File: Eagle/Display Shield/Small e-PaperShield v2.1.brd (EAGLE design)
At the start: 172.6 x 54.6 mm, 141 parts, among them J2 3300060P1-ST-TF-003A, J3 2.54-8p-male-SMD, J4 2.54-8p-male-SMD, J5 2.54-6p-male-SMD, J6 2.54-6p-male-SMD, J7 2.54-2x3p-female-SMD, Q10 MOSFET-P-044021001, Q11 2N7002, Q2 2N7002, Q3 MOSFET-P-044021001, Q5 MOSFET-P-044021001, Q7 MOSFET-P-044021001, Q8 2N7002, Q9 2N7002, SW1 BUTTON-4P-REINFORCE'TS-1188E', U2 XC6206-3.3-1300260P1, U3 74VHC125PW, U4 74VHC125PW, U5 GT20L16P1Y, U6 DNP, U7 EPD 1.44/2.0/2.7 inch, U8 DNP, U9 S-8120CNB-DRB-TF-G//200021001

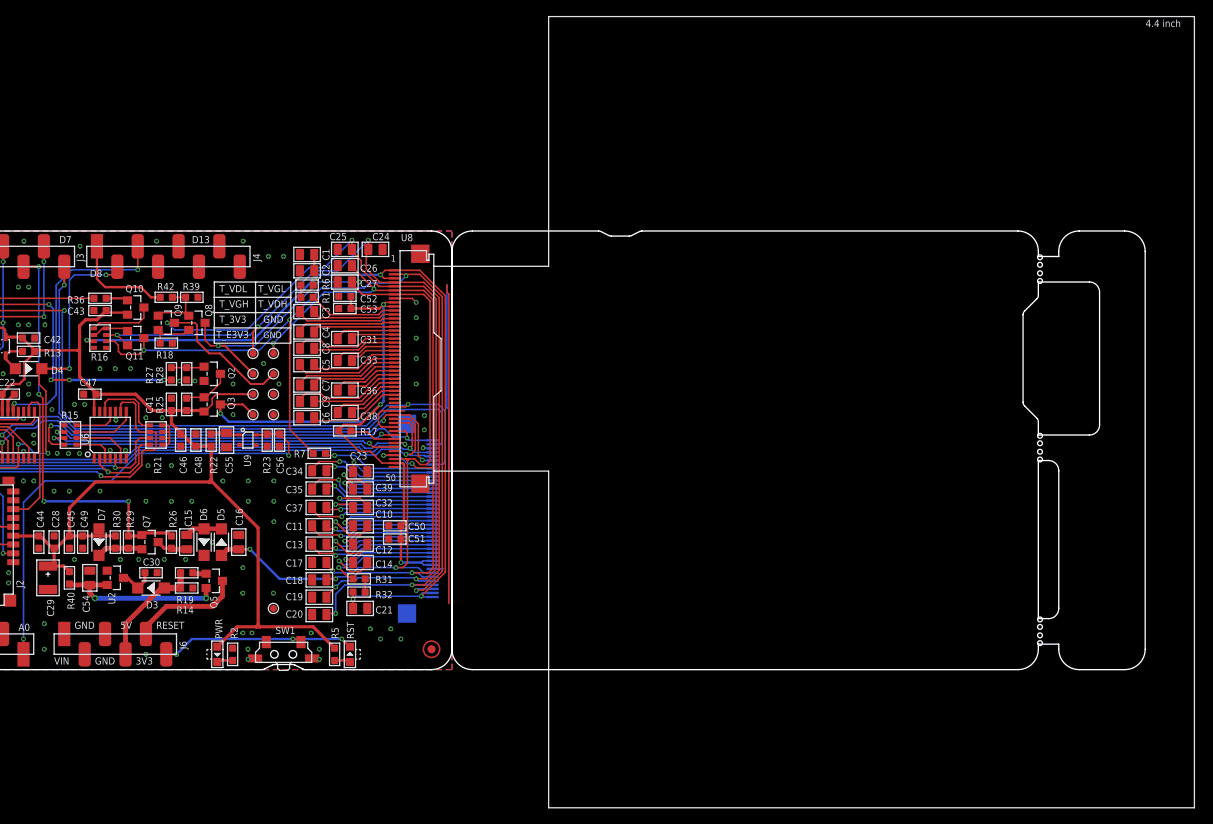
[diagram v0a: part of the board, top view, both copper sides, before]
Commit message: removed all unnecessary components of display shield
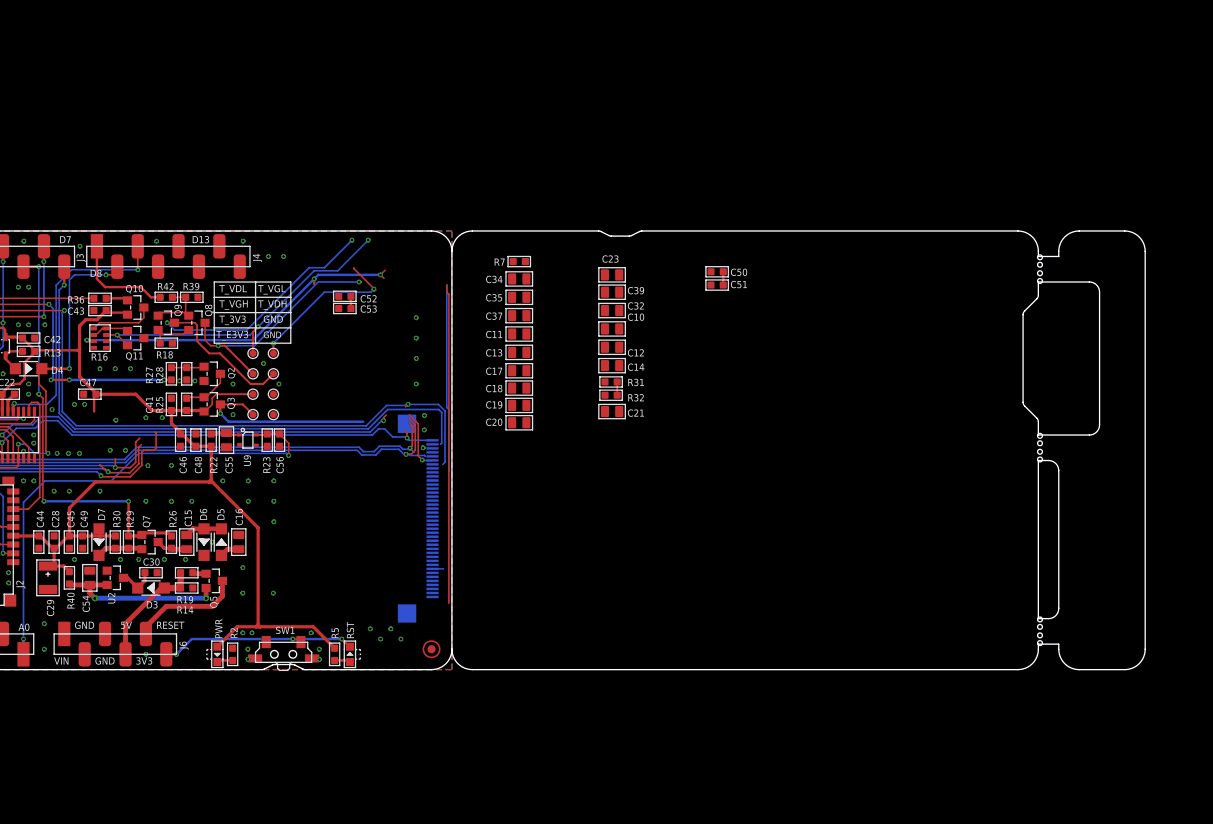
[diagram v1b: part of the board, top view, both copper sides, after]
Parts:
- removed C1, C2, C24, C25, C26, C27, C3, C31, C33, C36, C38, C4, C5, C6, C7, C8, C9: DNP, Discrete:C0805
- removed R1, R17, R6: DNP, Discrete:R0603
- removed R15, R21: DNP, Discrete:1206-8-3.3X2.4
- removed TP8: (no value), Discrete:TP_3535
- removed U6: DNP, IC:TSSOP14
- removed U8: DNP, template:50P-0.5
- moved C50 51.1 mm to (57.8, 22.2)
- moved C51 51.1 mm to (57.8, 20.6)
- moved C10 39.8 mm to (44.7, 15.1)
- moved C12 39.8 mm to (44.7, 12.8)
- moved C14 39.8 mm to (44.7, 10.5)
- moved C21 39.8 mm to (44.7, 4.83)
- moved C23 39.8 mm to (44.7, 21.8)
- moved C32 39.8 mm to (44.7, 17.4)
- moved C39 39.8 mm to (44.7, 19.7)
- moved R31 39.8 mm to (44.6, 8.51)
- moved R32 39.8 mm to (44.6, 6.86)
- moved C17 34.5 mm to (33.1, 9.91)
- moved C18 34.5 mm to (33.1, 7.75)
- moved C19 34.5 mm to (33.1, 5.59)
- moved C35 34.5 mm to (33.1, 19.1)
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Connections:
- removed net EPD_CKV: R15.7, U8.44
- removed net EPD_OE123: R15.8, U8.42
- removed net EPD_STV_IN: R15.6, U8.45
- removed net N$15: C4.1, U8.14
- removed net N$19: R21.5, U6.12
- removed net N$23: R15.1, U6.3
- removed net N$24: R15.3, U6.8
- removed net N$25: R15.4, U6.11
- removed net N$26: R15.2, U6.6
- removed net N$30: R1.2, R6.1
- removed net N$33: R15.5
- removed net N$39: C4.2, U8.15
- removed net N$40: C3.1, U8.12
- removed net N$41: C31.2, U8.17
- removed net N$42: C31.1, U8.16
- removed net N$43: C8.1, U8.18
- removed net N$44: C8.2, U8.19
- removed net N$45: C33.2, U8.21
- removed net N$46: C33.1, U8.20
- removed net N$47: C5.1, U8.22
- removed net N$48: C5.2, U8.23
- removed net N$49: C7.1, U8.24
- removed net N$50: C7.2, U8.25
- removed net N$51: C36.1, U8.26
- removed net N$52: C36.2, U8.27
- removed net N$53: C9.1, U8.28
- removed net N$54: C9.2, U8.29
- removed net N$55: C38.1, U8.30
- removed net N$56: C38.2, U8.31
- removed net N$57: C6.1, U8.32
- removed net N$58: R1.1, U8.11
- removed net N$67: R17.1, U8.43
- removed net N$82: C3.2, U8.13
- net /EPD_CS: no longer U8.41
- net EPD_/RESET: no longer U8.35
- net EPD_BORDER: no longer U8.2
- net EPD_SO: no longer U8.37
- net EPD_VCOM_PANEL: no longer C1.1, C2.1, R6.2, U8.1, U8.3
- net EPD_VDH: no longer C25.1, U8.5
- net EPD_VDL: no longer C24.1, U8.4
- net EPD_VGH: no longer C27.1, U8.48, U8.7
- net EPD_VGL: no longer C26.1, U8.47, U8.6
- net GND: no longer C1.2, C2.2, C24.2, C25.2, C26.2, C27.2, C6.2, R21.1, R21.2, R21.3, R21.4, TP8.T, U6.1, U6.10, U6.13, U6.4, U6.7, U8.36, U8.40, U8.50, U8.8, U8.P1, U8.P2
- net M_CKV: no longer R21.7, U6.5
- net M_OE123: no longer R21.8, U6.2
- net M_STV_IN: no longer R21.6, U6.9
- net S_MOSI: no longer U8.38
- net S_SCK: no longer U8.39
- net VCC_3V3: no longer U6.14
- net VCC_3V3_EPD: no longer R17.2, U8.10, U8.49, U8.9
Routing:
- net EPD_BORDER: track 109.7 -> 0.00 mm, vias 4 -> 0
- net EPD_VGL: track 103.0 -> 23.0 mm, vias 7 -> 2
- net EPD_VDL: track 111.9 -> 43.3 mm, vias 5 -> 3
- net EPD_VGH: track 96.8 -> 30.7 mm, vias 4 -> 2
- net EPD_VDH: track 112.1 -> 46.1 mm, vias 4 -> 2
- net EPD_VCOM_PANEL: track 108.8 -> 42.9 mm, vias 5 -> 3
- net VCC_3V3_EPD: track 82.8 -> 27.1 mm, vias 4 -> 1
- net EPD_OE123: track 47.8 -> 0.00 mm, vias 2 -> 0
- net EPD_CKV: track 47.1 -> 0.00 mm, vias 2 -> 0
- net EPD_STV_IN: track 43.9 -> 0.00 mm, vias 2 -> 0
- net N$97: track 18.0 -> 0.00 mm, vias 1 -> 0
- net N$93: track 18.0 -> 0.00 mm, vias 1 -> 0
- net N$101: track 17.1 -> 0.00 mm, vias 1 -> 0
- net N$81: track 16.6 -> 0.00 mm, vias 1 -> 0
- net GND: track 85.3 -> 68.7 mm, vias 113 -> 112
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
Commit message: re-placed components to board area, added 40pin connector. ready to go
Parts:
- added X1: FH12-40S-0.5SH, con-hirose:FH12-40S-0.5SH
- moved S5 203.7 mm to (84.5, 12.4)
- moved S6 203.7 mm to (74.7, 12.4)
- moved S7 203.7 mm to (64.9, 12.4)
- moved S8 203.7 mm to (55.1, 12.4)
- moved C11 76.2 mm to (85.5, 69.8)
- moved C13 76.2 mm to (85.5, 67.5)
- moved C17 76.2 mm to (85.5, 65.2)
- moved C18 76.2 mm to (85.5, 63.0)
- moved C19 76.2 mm to (85.5, 60.9)
- moved C20 76.2 mm to (85.5, 58.7)
- moved C34 76.2 mm to (85.5, 76.6)
- moved C35 76.2 mm to (85.5, 74.3)
- moved C37 76.2 mm to (85.5, 72.1)
- moved C15 75.1 mm to (47.6, 38.8)
- moved C16 75.1 mm to (54.1, 38.8)
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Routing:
- net /EPD_CS: track 67.1 -> 64.2 mm
- net GND: track 68.7 -> 67.3 mm
- net EPD_SO: track 61.5 -> 60.3 mm
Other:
- board size 172.6 x 54.6 mm -> 86.3 x 54.6 mm

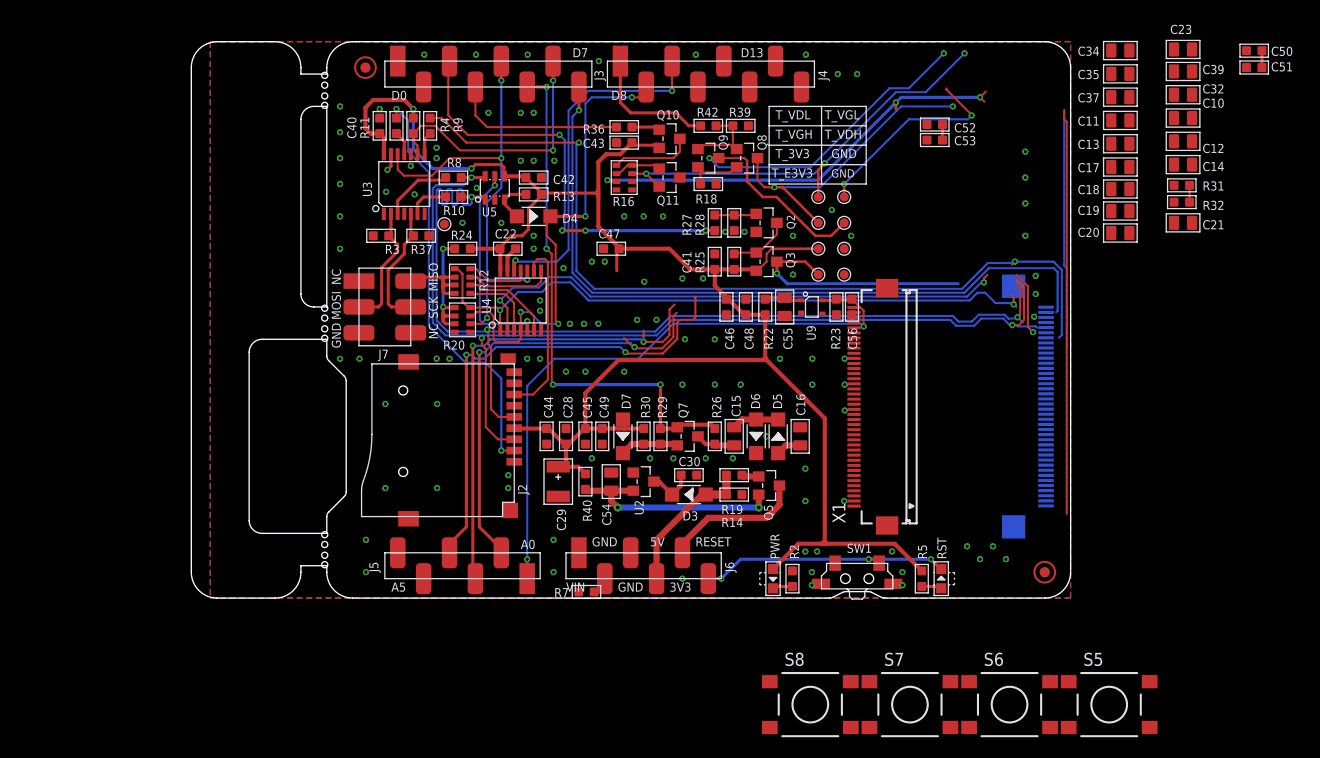
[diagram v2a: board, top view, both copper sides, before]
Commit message: reshaped board, snapped components to grid.
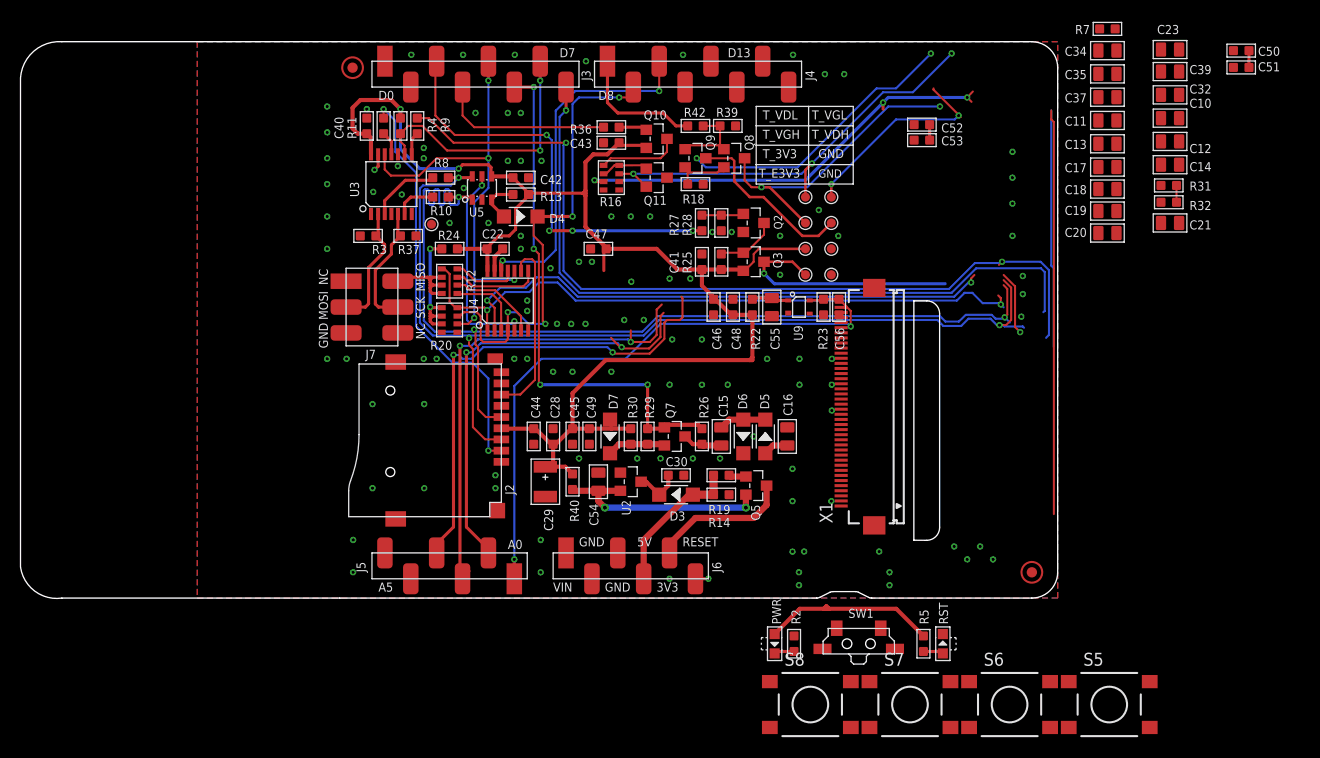
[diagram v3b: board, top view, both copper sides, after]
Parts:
- removed U7: EPD 1.44/2.0/2.7 inch, moudle:40P-0.5
- moved R7 75.3 mm to (84.3, 78.8)
- moved PWR 6.39 mm to (51.6, 18.4)
- moved R2 6.39 mm to (53.5, 18.4)
- moved R5 6.39 mm to (66.2, 18.4)
- moved RST 6.39 mm to (68.1, 18.4)
- moved SW1 6.39 mm to (59.9, 18.4)
- moved R31 1.28 mm to (90.3, 63.4)
- moved R32 1.28 mm to (90.3, 61.7)
- moved C10 1.28 mm to (90.4, 70.0)
- moved C12 1.28 mm to (90.4, 67.7)
- moved C14 1.28 mm to (90.4, 65.4)
- moved C21 1.28 mm to (90.4, 59.7)
- moved C23 1.28 mm to (90.4, 76.7)
- moved C32 1.28 mm to (90.4, 72.3)
- moved C39 1.28 mm to (90.4, 74.6)
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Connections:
- net /EPD_CS: now also X1.40; no longer U7.1
- net ADC_IN: now also X1.33; no longer U7.8
- net EPD_/RESET: now also X1.34; no longer U7.7
- net EPD_BORDER: now also X1.3; no longer U7.38
- net EPD_SO: now also X1.35; no longer U7.6
- net EPD_VCL: now also X1.32; no longer U7.9
- net EPD_VCOM_PANEL: now also X1.1, X1.2; no longer U7.39, U7.40
- net EPD_VDH: now also X1.5; no longer U7.36
- net EPD_VDL: now also X1.4; no longer U7.37
- net EPD_VGH: now also X1.7; no longer U7.34
- net EPD_VGL: now also X1.6; no longer U7.35
- net GND: now also X1.38, X1.8; no longer U7.3, U7.33, U7.P1, U7.P2
- net M_EPD_BUSY: now also X1.39; no longer U7.2
- net N$100: now also X1.13; no longer U7.28
- net N$101: now also X1.12; no longer U7.29
- net N$34: now also X1.31; no longer U7.10
- net N$35: now also X1.30; no longer U7.11
- net N$36: now also X1.29; no longer U7.12
- net N$37: now also X1.28; no longer U7.13
- net N$81: now also X1.27; no longer U7.14
- net N$85: now also X1.26; no longer U7.15
- net N$88: now also X1.25; no longer U7.16
- net N$89: now also X1.24; no longer U7.17
- net N$90: now also X1.23; no longer U7.18
- net N$91: now also X1.22; no longer U7.19
- net N$92: now also X1.21; no longer U7.20
- net N$93: now also X1.20; no longer U7.21
- net N$94: now also X1.19; no longer U7.22
- net N$95: now also X1.18; no longer U7.23
- net N$96: now also X1.17; no longer U7.24
- net N$97: now also X1.16; no longer U7.25
- net N$98: now also X1.15; no longer U7.26
- net N$99: now also X1.14; no longer U7.27
- net S_MOSI: now also X1.36; no longer U7.5
- net S_SCK: now also X1.37; no longer U7.4
- net VCC_3V3_EPD: now also X1.10, X1.9; no longer U7.31, U7.32
- net VCOM_DRIVER: now also X1.11; no longer U7.30
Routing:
- net M_RESET: track 25.4 -> 1.27 mm, vias 3 -> 1
- net VCC_3V3: track 184.9 -> 164.4 mm
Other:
- board size 86.3 x 54.6 mm -> 101.8 x 54.6 mm

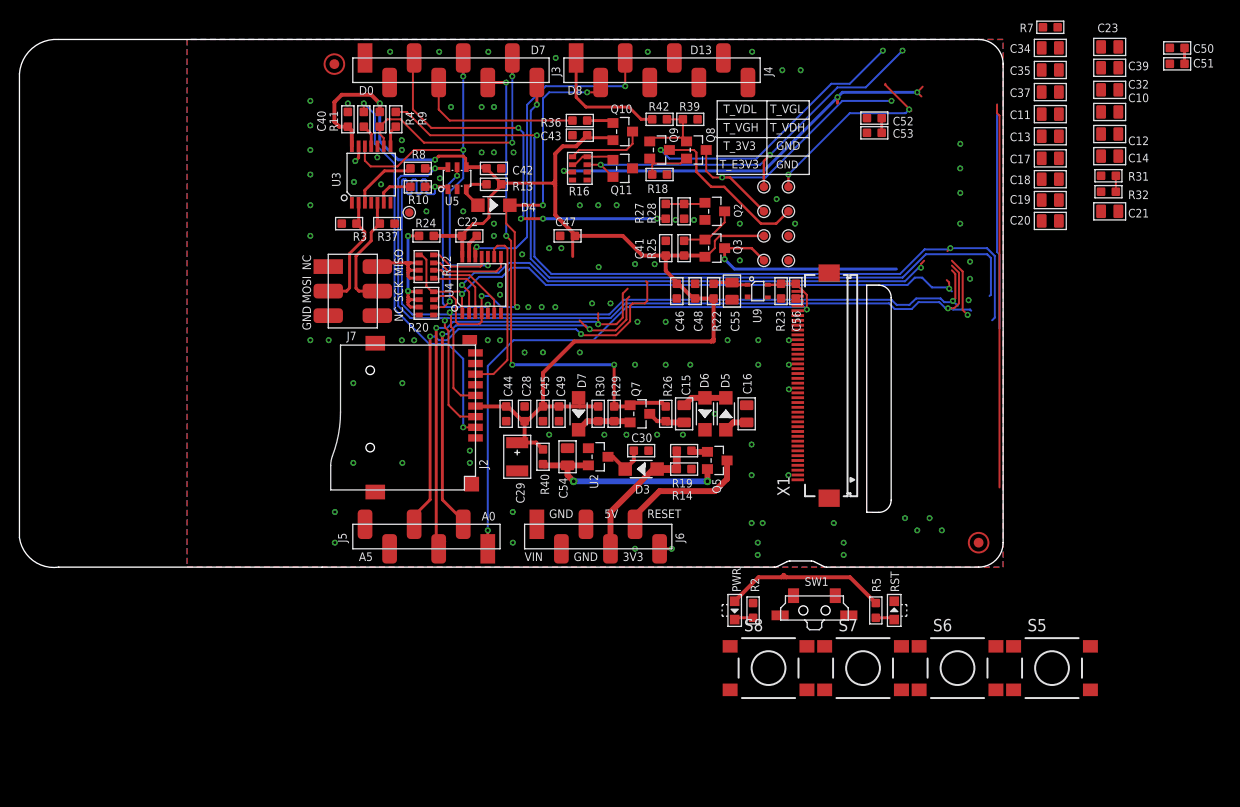
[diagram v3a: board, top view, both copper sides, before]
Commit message: re-routed most of the traces
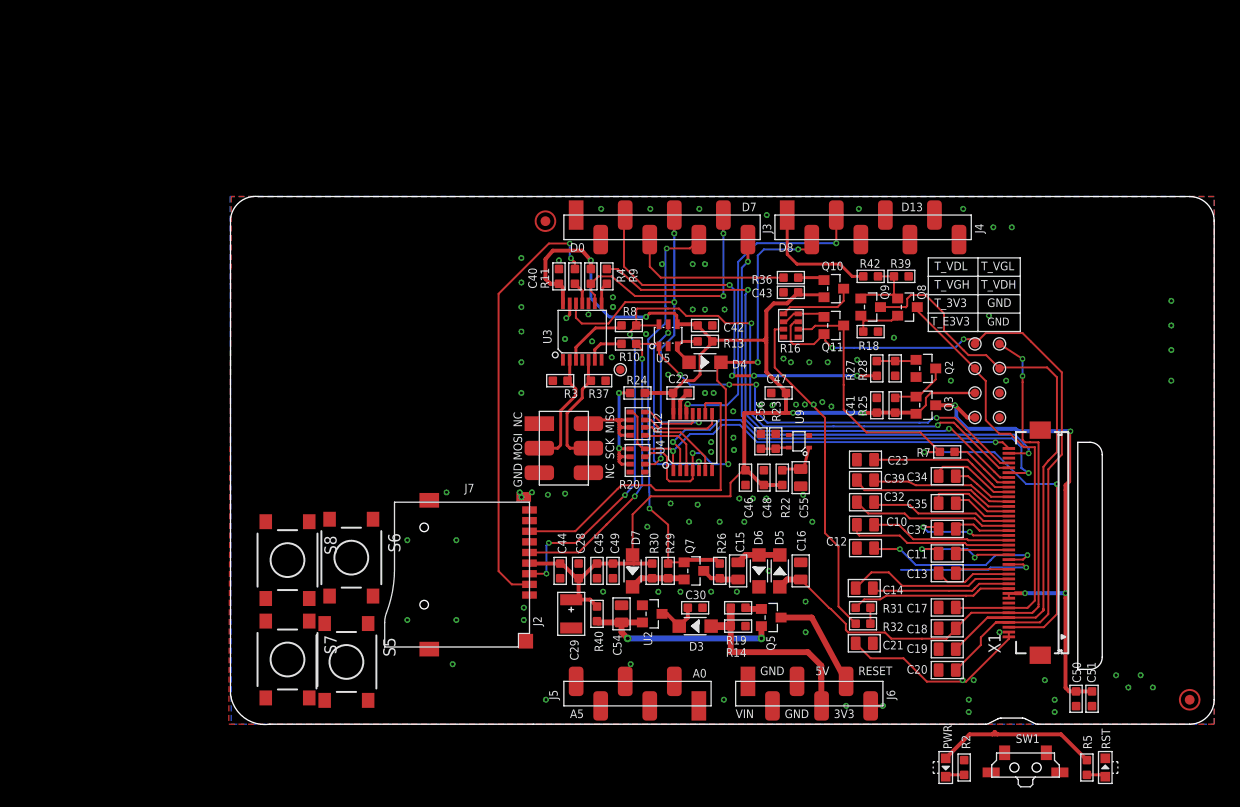
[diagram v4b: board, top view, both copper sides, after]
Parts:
- removed C52, C53: 100nF, Discrete:C0603
- moved S5 73.0 mm to (11.4, 13.1), turned to 270 degrees
- moved C50 68.2 mm to (86.9, 9.27), turned to 90 degrees
- moved C51 66.3 mm to (88.6, 9.27), turned to 90 degrees
- moved S6 63.8 mm to (11.9, 23.9), turned to 270 degrees
- moved S7 59.6 mm to (5.33, 13.3), turned to 270 degrees
- moved C14 51.4 mm to (65.0, 20.7)
- moved C21 51.4 mm to (65.0, 15.0)
- moved R31 51.4 mm to (64.9, 18.7)
- moved R32 51.4 mm to (64.9, 17.0)
- moved S8 51.0 mm to (5.33, 23.6), turned to 270 degrees
- moved C12 49.7 mm to (65.2, 24.9), turned to 180 degrees
- moved C23 49.6 mm to (65.2, 34.0), turned to 0 degrees
- moved C10 49.6 mm to (65.2, 27.3), turned to 180 degrees
- moved C32 49.6 mm to (65.2, 29.6)
- moved C39 49.6 mm to (65.2, 31.9)
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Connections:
- net GND: no longer C52.1, C53.1
- net VCC_3V3_EPD: no longer C52.2, C53.2
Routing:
- net GND: track 67.3 -> 4.16 mm, vias 112 -> 105
- net EPD_BORDER: track 0.00 -> 61.0 mm, vias 0 -> 2
- net M_TEMP_SEN: track 60.6 -> 2.92 mm, vias 2 -> 0
- net M_CKV: track 48.7 -> 0.00 mm, vias 2 -> 0
- net M_STV_IN: track 48.1 -> 0.00 mm, vias 2 -> 0
- net M_OE123: track 45.5 -> 0.00 mm, vias 2 -> 0
- net EPD_VGL: track 23.0 -> 61.4 mm
- net EPD_VDL: track 43.3 -> 74.6 mm, vias 3 -> 2
- net VCC_3V3_EPD: track 27.1 -> 56.0 mm, vias 1 -> 4
- net EPD_/RESET: track 85.3 -> 58.5 mm
- net S_SCK: track 100.5 -> 75.8 mm, vias 3 -> 6
- net M_EPD_BUSY: track 72.1 -> 52.2 mm, vias 1 -> 2
- net N$96: track 0.00 -> 19.1 mm, vias 0 -> 2
- net /EPD_CS: track 64.2 -> 46.7 mm
- net N$100: track 0.00 -> 17.4 mm
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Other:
- board size 101.8 x 54.6 mm -> 101.8 x 54.7 mm
